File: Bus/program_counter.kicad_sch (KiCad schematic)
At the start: 2 parts, among them J6 Conn_01x08_Pin, J7 Conn_01x06_Pin

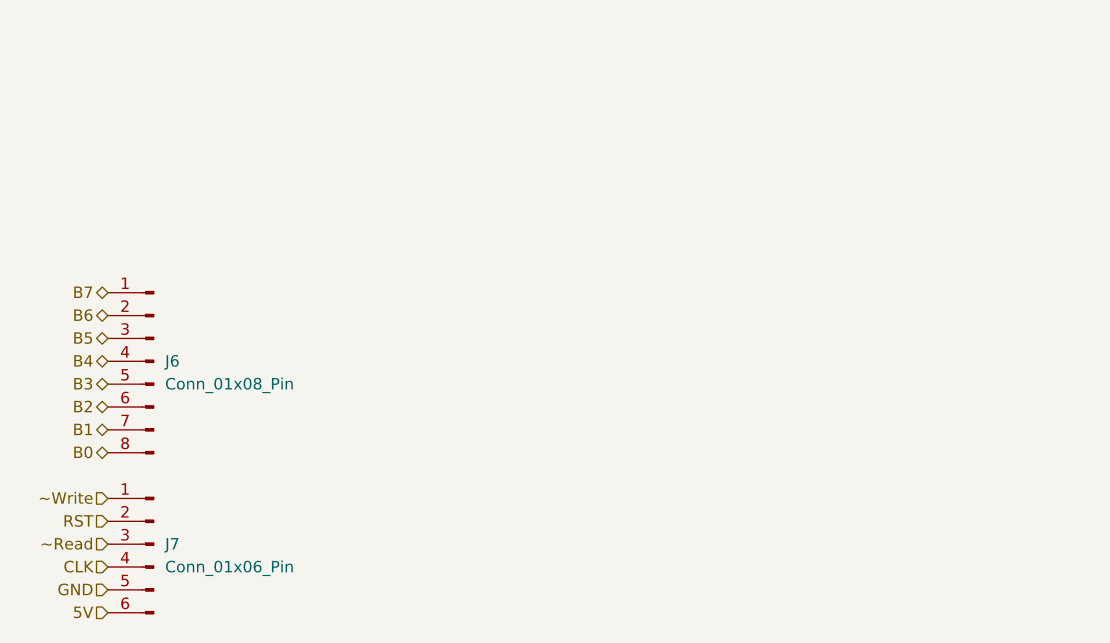
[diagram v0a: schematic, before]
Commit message: Some initial bus layout
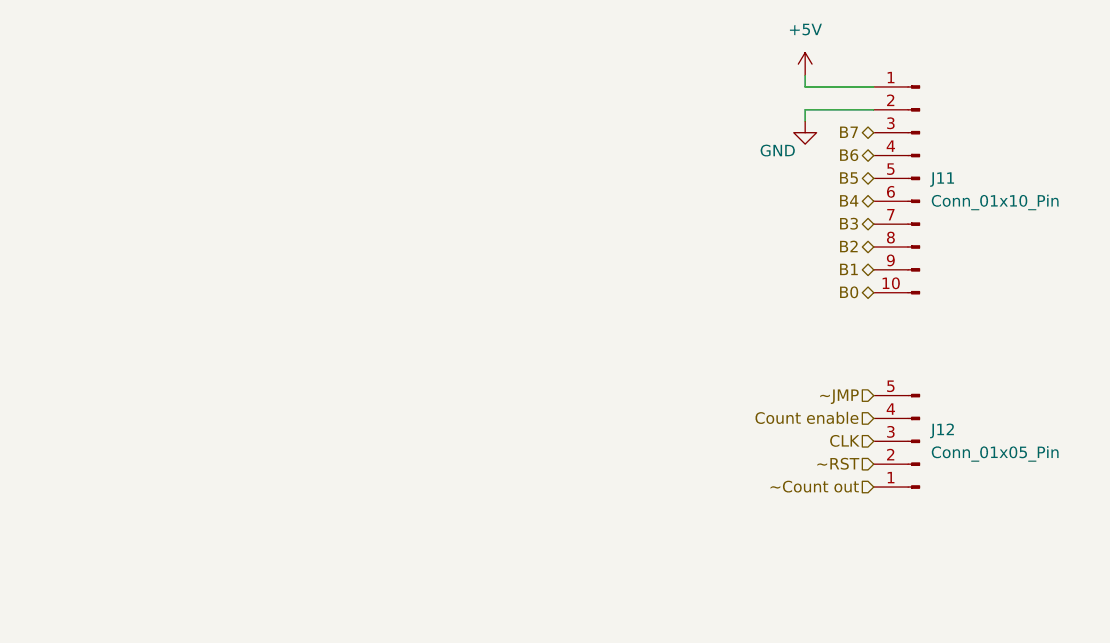
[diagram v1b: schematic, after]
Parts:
- removed J6: Conn_01x08_Pin, Connector_PinHeader_2.54mm:PinHeader_1x08_P2.54mm_Vertical, symbol Connector:Conn_01x08_Pin
- removed J7: Conn_01x06_Pin, Connector_PinHeader_2.54mm:PinHeader_1x06_P2.54mm_Vertical, symbol Connector:Conn_01x06_Pin
- added J11: Conn_01x10_Pin, Connector_PinHeader_2.54mm:PinHeader_1x10_P2.54mm_Vertical, symbol Connector:Conn_01x10_Pin
- added J12: Conn_01x05_Pin, Connector_PinHeader_2.54mm:PinHeader_1x05_P2.54mm_Vertical, symbol Connector:Conn_01x05_Pin
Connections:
- net B0: now also J11.10 (Pin_10)
- net B1: now also J11.9 (Pin_9)
- net B2: now also J11.8 (Pin_8)
- net B3: now also J11.7 (Pin_7)
- net B4: now also J11.6 (Pin_6)
- net B5: now also J11.5 (Pin_5)
- net B6: now also J11.4 (Pin_4)
- net B7: now also J11.3 (Pin_3)
- net CLK: now also J12.3 (Pin_3)
- net GND: now also J11.2 (Pin_2)
- new net +5V: J11.1 (Pin_1)
- new net Count enable: J12.4 (Pin_4)
- new net ~Count out: J12.1 (Pin_1)
- new net ~JMP: J12.5 (Pin_5)
- new net ~RST: J12.2 (Pin_2)

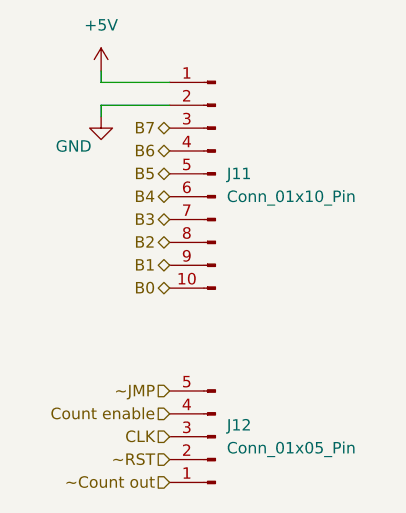
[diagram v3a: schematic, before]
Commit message: Updated bus schmatic pins to match final layouts
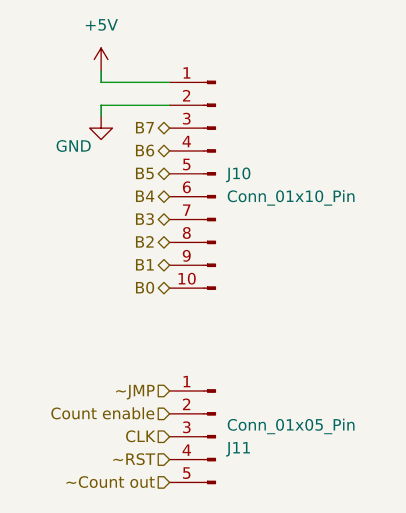
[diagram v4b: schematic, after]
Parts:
- renumbered J11 to J10, J12 to J11
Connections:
- net Count enable: now also J11.2 (Pin_2); no longer J11.4 (Pin_4)
- net ~Count out: now also J11.5 (Pin_5); no longer J11.1 (Pin_1)
- net ~JMP: now also J11.1 (Pin_1); no longer J11.5 (Pin_5)
- net ~RST: now also J11.4 (Pin_4); no longer J11.2 (Pin_2)
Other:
- moved on the sheet: J11
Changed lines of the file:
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@@
 	(symbol
 		(lib_id "Connector:Conn_01x05_Pin")
-		(at 161.29 95.25 180)
-		(unit 1)
-		(exclude_from_sim no)
-		(in_bom yes)
-		(on_board yes)
-		(dnp no)
-		(fields_autoplaced yes)
-		(property "Reference" "J12"
-			(at 162.56 93.9799 0)
+		(at 161.29 95.25 0)
+		(mirror y)
+		(unit 1)
+		(exclude_from_sim no)
+		(in_bom yes)
+		(on_board yes)
+		(dnp no)
+		(property "Reference" "J11"
+			(at 162.56 96.5201 0)
 			(effects
 				(font
@@
 		)
 		(property "Value" "Conn_01x05_Pin"
-			(at 162.56 96.5199 0)
+			(at 162.56 93.9801 0)
 			(effects
 				(font
@@
 			(project "bus"
 				(path "/37ae8b13-e183-404e-b70a-681e1af60f55/707279f8-562c-4ee0-b713-f923a04fe364"
-					(reference "J12")
+					(reference "J11")
 					(unit 1)
 				)
@@
 		(dnp no)
 		(fields_autoplaced yes)
-		(property "Reference" "J11"
+		(property "Reference" "J10"
 			(at 162.56 66.0399 0)
 			(effects
@@
 			(project "bus"
 				(path "/37ae8b13-e183-404e-b70a-681e1af60f55/707279f8-562c-4ee0-b713-f923a04fe364"
-					(reference "J11")
+					(reference "J10")
 					(unit 1)
 				)
@@
 		(on_board yes)
 		(dnp no)
-		(property "Reference" "#PWR017"
+		(property "Reference" "#PWR014"
 			(at 148.59 66.04 0)
 			(effects
@@
 			(project "bus"
 				(path "/37ae8b13-e183-404e-b70a-681e1af60f55/707279f8-562c-4ee0-b713-f923a04fe364"
-					(reference "#PWR017")
+					(reference "#PWR014")
 					(unit 1)
 				)
@@
 		(dnp no)
 		(fields_autoplaced yes)
-		(property "Reference" "#PWR016"
+		(property "Reference" "#PWR013"
 			(at 148.59 58.42 0)
 			(effects
@@
 			(project "bus"
 				(path "/37ae8b13-e183-404e-b70a-681e1af60f55/707279f8-562c-4ee0-b713-f923a04fe364"
-					(reference "#PWR016")
-					(unit 1)
-				)
+					(reference "#PWR013")
+					(unit 1)
+				)
